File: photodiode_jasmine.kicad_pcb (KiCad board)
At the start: 2 copper layers, 23 parts, among them U1 74HCT4051, U2 74HCT4051, U3 74HCT4051, U4 MCP6004

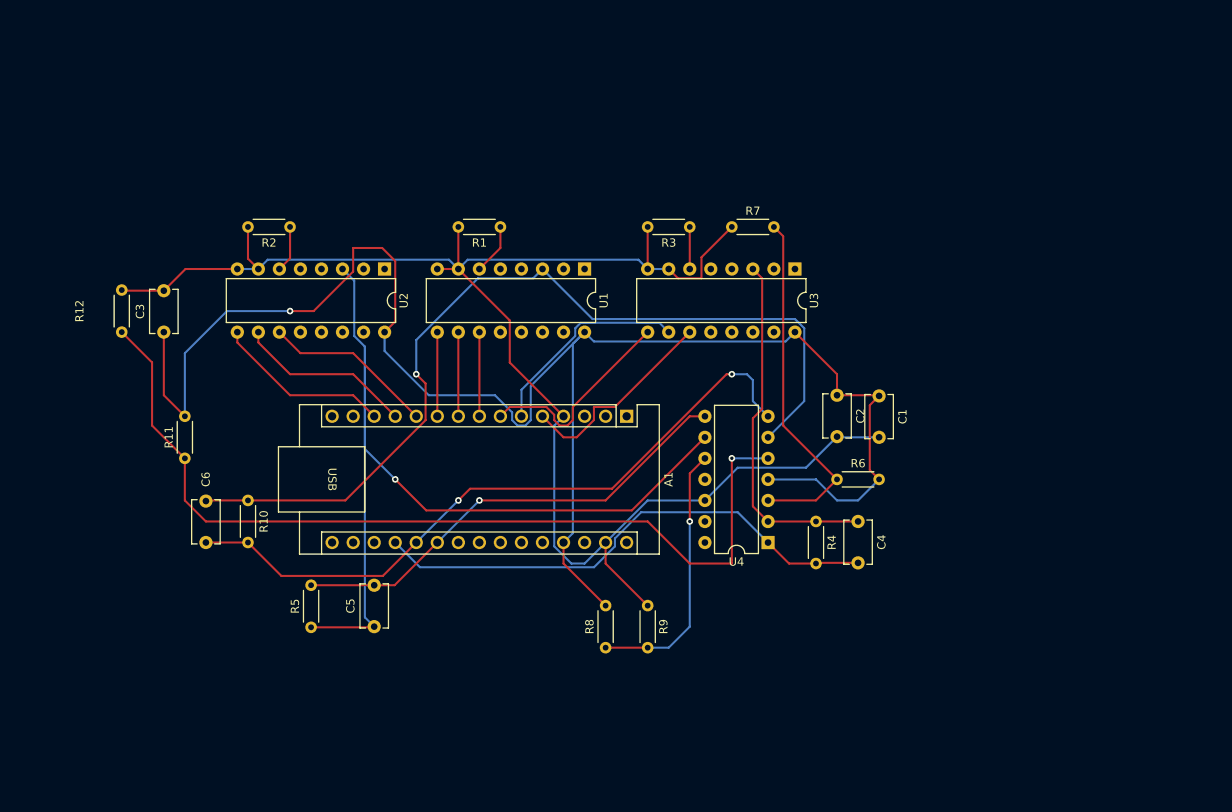
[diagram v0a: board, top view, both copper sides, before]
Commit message: Added photodiode connector, haven't routed
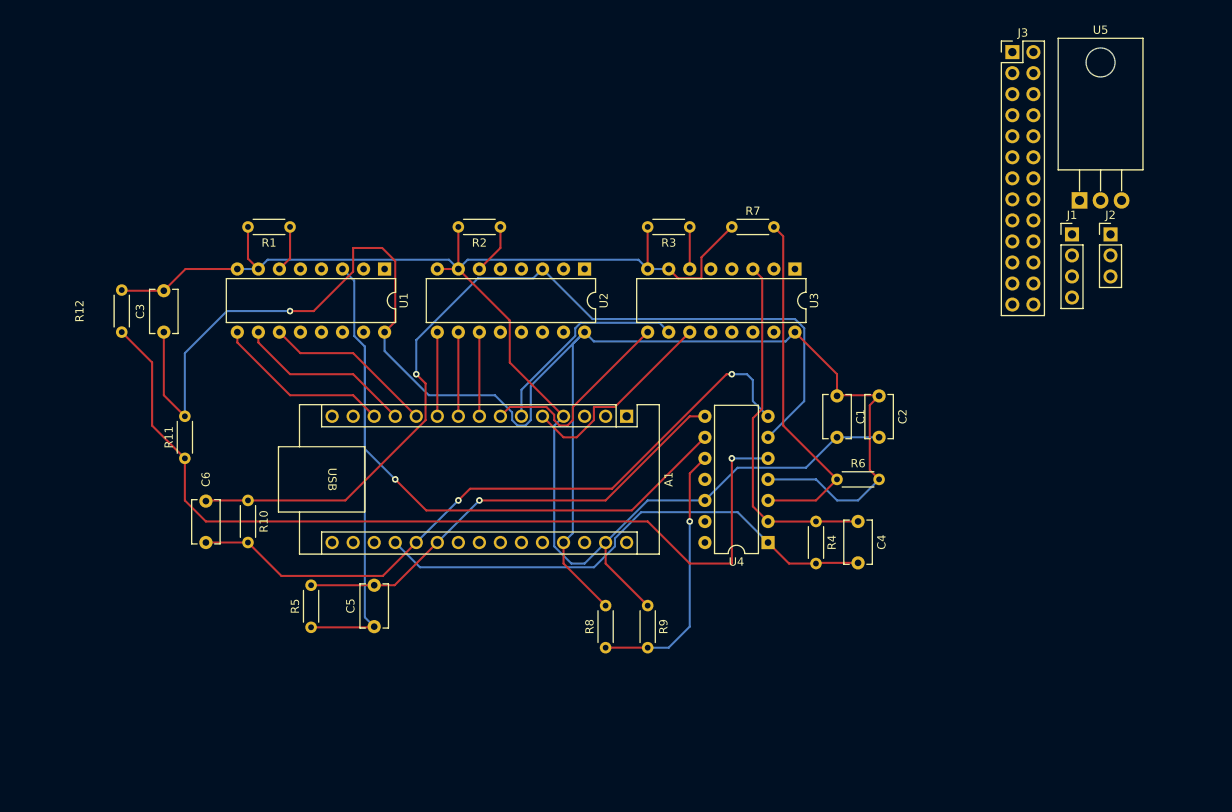
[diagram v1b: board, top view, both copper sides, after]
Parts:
- added J1: Conn_01x04_Pin, Connector_PinHeader_2.54mm:PinHeader_1x04_P2.54mm_Vertical, F.Cu at (218.9, 79.6)
- added J2: Conn_01x03_Pin, Connector_PinHeader_2.54mm:PinHeader_1x03_P2.54mm_Vertical, F.Cu at (223.5, 79.6)
- added J3: Conn_02x13_Top_Bottom, Connector_PinHeader_2.54mm:PinHeader_2x13_P2.54mm_Vertical, F.Cu at (211.7, 57.6)
- added U5: L7805, Package_TO_SOT_THT:TO-220-3_Horizontal_TabDown, F.Cu at (219.8, 75.5)
- moved R1 25.4 mm to (124.5, 78.7)
- moved R2 25.4 mm to (149.9, 78.7)
- moved U1 24.1 mm to (135.9, 83.8)
- moved U2 24.1 mm to (160.0, 83.8)
- moved C2 5.08 mm to (195.6, 99.1)
- moved C1 5.08 mm to (190.5, 99.1)
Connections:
- A1 pad 14: unconnected-(A1-MOSI-Pad14) -> /LED_Data
- C5 pad 1: /Amp/PhotodiodesMuxed3/Out -> /Amp/PhotodiodesMuxed2/Out
- C6 pad 1: /Amp/PhotodiodesMuxed2/Out -> /Amp/PhotodiodesMuxed3/Out
- R10 pad 1: /Amp/PhotodiodesMuxed2/Out -> /Amp/PhotodiodesMuxed3/Out
- R5 pad 1: /Amp/PhotodiodesMuxed3/Out -> /Amp/PhotodiodesMuxed2/Out
- U1 pad 1: /Amp/PhotodiodesMuxed2/p5 -> PD13
- U1 pad 10: /Amp/Mux2SelB -> /Amp/Mux3SelB
- U1 pad 11: /Amp/Mux2SelA -> /Amp/Mux3SelA
- U1 pad 12: /Amp/PhotodiodesMuxed2/p4 -> PD12
- U1 pad 13: /Amp/PhotodiodesMuxed2/p1 -> PD9
- U1 pad 14: /Amp/PhotodiodesMuxed2/p2 -> PD10
- U1 pad 15: /Amp/PhotodiodesMuxed2/p3 -> PD11
- U1 pad 2: /Amp/PhotodiodesMuxed2/p7 -> PD15
- U1 pad 4: /Amp/PhotodiodesMuxed2/p8 -> PD16
- U1 pad 5: /Amp/PhotodiodesMuxed2/p6 -> PD14
- U1 pad 9: /Amp/Mux2SelC -> /Amp/Mux3SelC
- U2 pad 1: /Amp/PhotodiodesMuxed3/p5 -> PD21
- U2 pad 10: /Amp/Mux3SelB -> /Amp/Mux2SelB
- U2 pad 11: /Amp/Mux3SelA -> /Amp/Mux2SelA
- U2 pad 12: /Amp/PhotodiodesMuxed3/p4 -> PD20
- U2 pad 13: /Amp/PhotodiodesMuxed3/p1 -> PD17
- U2 pad 14: /Amp/PhotodiodesMuxed3/p2 -> PD18
- U2 pad 15: /Amp/PhotodiodesMuxed3/p3 -> PD19
- U2 pad 2: /Amp/PhotodiodesMuxed3/p7 -> PD23
- U2 pad 4: /Amp/PhotodiodesMuxed3/p8 -> PD24
- U2 pad 5: /Amp/PhotodiodesMuxed3/p6 -> PD22
- U2 pad 9: /Amp/Mux3SelC -> /Amp/Mux2SelC
- U3 pad 1: /Amp/PhotodiodesMuxed1/p5 -> PD5
- U3 pad 12: /Amp/PhotodiodesMuxed1/p4 -> PD4
- U3 pad 13: /Amp/PhotodiodesMuxed1/p1 -> PD1
- U3 pad 14: /Amp/PhotodiodesMuxed1/p2 -> PD2
- U3 pad 15: /Amp/PhotodiodesMuxed1/p3 -> PD3
- U3 pad 2: /Amp/PhotodiodesMuxed1/p7 -> PD7
- U3 pad 4: /Amp/PhotodiodesMuxed1/p8 -> PD8
- U3 pad 5: /Amp/PhotodiodesMuxed1/p6 -> PD6
- U4 pad 6: /Amp/PhotodiodesMuxed2/Out -> /Amp/PhotodiodesMuxed3/Out
- U4 pad 9: /Amp/PhotodiodesMuxed3/Out -> /Amp/PhotodiodesMuxed2/Out
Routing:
- net /Amp/PhotodiodesMuxed3/Out: track 112.6 -> 109.1 mm
- net /Amp/PhotodiodesMuxed2/Out: track 109.1 -> 112.6 mm
- net Net-(U2-~{E}): track 5.61 -> 6.13 mm
- net Net-(U1-~{E}): track 6.13 -> 5.61 mm

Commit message: Add connectors, routed
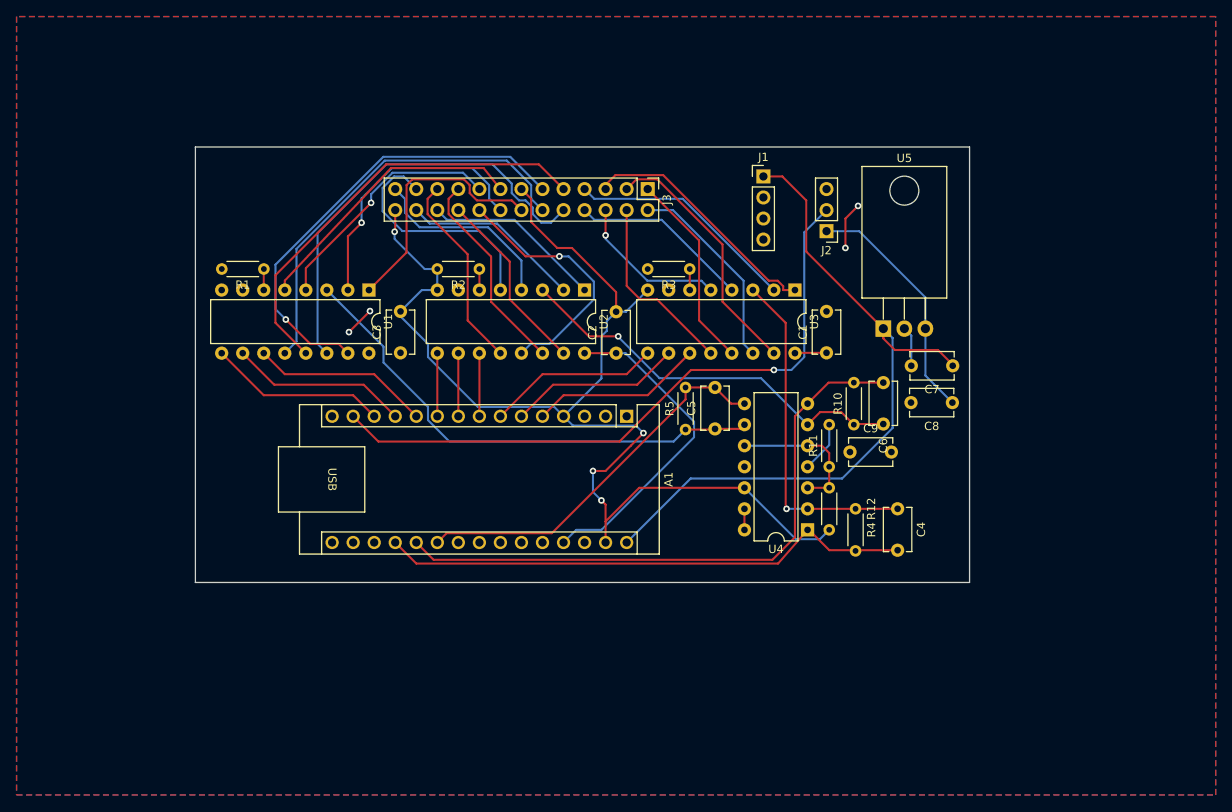
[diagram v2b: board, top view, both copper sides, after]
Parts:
- removed R6, R8: 1M, Resistor_THT:R_Axial_DIN0204_L3.6mm_D1.6mm_P5.08mm_Horizontal
- removed R7, R9: 10k, Resistor_THT:R_Axial_DIN0204_L3.6mm_D1.6mm_P5.08mm_Horizontal
- added C7: 0.33u, Capacitor_THT:C_Disc_D5.1mm_W3.2mm_P5.00mm, F.Cu at (204.5, 95.5)
- added C8: 0.1u, Capacitor_THT:C_Disc_D5.1mm_W3.2mm_P5.00mm, F.Cu at (204.4, 99.9)
- added C9: 0.1u, Capacitor_THT:C_Disc_D5.1mm_W3.2mm_P5.00mm, F.Cu at (192.1, 105.9)
- moved R12 90.2 mm to (189.6, 115.3), turned to 90 degrees
- moved C6 82.3 mm to (196.1, 102.5), turned to 90 degrees
- moved R11 77.8 mm to (189.6, 107.7)
- moved R10 73.7 mm to (192.5, 102.6), turned to 90 degrees
- moved R5 51.1 mm to (172.2, 103.2)
- moved C5 47.6 mm to (175.8, 103.1)
- moved J3 47.0 mm to (167.6, 74.2), turned to -90 degrees
- moved J1 37.9 mm to (181.6, 72.6)
- moved J2 34.3 mm to (189.2, 79.2), turned to 180 degrees
- moved C2 32.2 mm to (163.8, 94.0), turned to 90 degrees
- moved C3 28.7 mm to (137.8, 93.9)
- moved U5 28.3 mm to (196.1, 91.0)
- moved R1 5.98 mm to (121.3, 83.8)
- moved R2 5.68 mm to (147.3, 83.8)
- moved C1 5.35 mm to (189.2, 93.9), turned to 90 degrees
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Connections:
- R11 pad 1: Net-(U4B-+) -> /Amp/Vref
- R12 pad 2: Net-(U4B-+) -> /Amp/Vref
- U4 pad 10: Net-(U4C-+) -> /Amp/Vref
- U4 pad 3: Net-(U4A-+) -> /Amp/Vref
- U4 pad 5: Net-(U4B-+) -> /Amp/Vref
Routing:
- net +5V: track 202.6 -> 58.8 mm, vias 1 -> 4
- net Net-(U4B-+): track 109.7 -> 0.00 mm, vias 1 -> 0
- net +12V: track 0.00 -> 88.1 mm
- net /LED_Data: track 0.00 -> 78.8 mm, vias 0 -> 1
- net /Amp/PhotodiodesMuxed3/Out: track 109.1 -> 49.1 mm
- net PD11: track 0.00 -> 55.6 mm, vias 0 -> 1
- net PD10: track 0.00 -> 52.8 mm
- net PD9: track 0.00 -> 52.5 mm
- net /Amp/PhotodiodesMuxed2/Out: track 112.6 -> 60.8 mm, vias 1 -> 0
- net PD12: track 0.00 -> 50.7 mm
- net GND: track 194.9 -> 148.9 mm, vias 0 -> 4
- net Net-(U4A-+): track 42.3 -> 0.00 mm
- net PD14: track 0.00 -> 34.3 mm
- net PD15: track 0.00 -> 33.1 mm, vias 0 -> 1
- net Net-(U4C-+): track 32.3 -> 0.00 mm, vias 1 -> 0
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- added copper zone on B.Cu, net +5V
- added copper zone on F.Cu, net GND
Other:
- board outline added: 93.5 x 52.6 mm
